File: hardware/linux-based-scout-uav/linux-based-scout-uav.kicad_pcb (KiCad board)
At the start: 2 copper layers, 70 x 100 mm, 40 parts, among them J1 XT60PW-M, J2 Micro_SD_Card_Det2, J3 TC2050-IDC-NL, J4 0786463001, J5 GSB1C41110SSHR, Q1 DMP3013SFV, Q2 DMP3013SFV, U1 OSD32MP157C-512M-IAA, U10 G313-06329-00, U2 RN2903A-I_RM098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

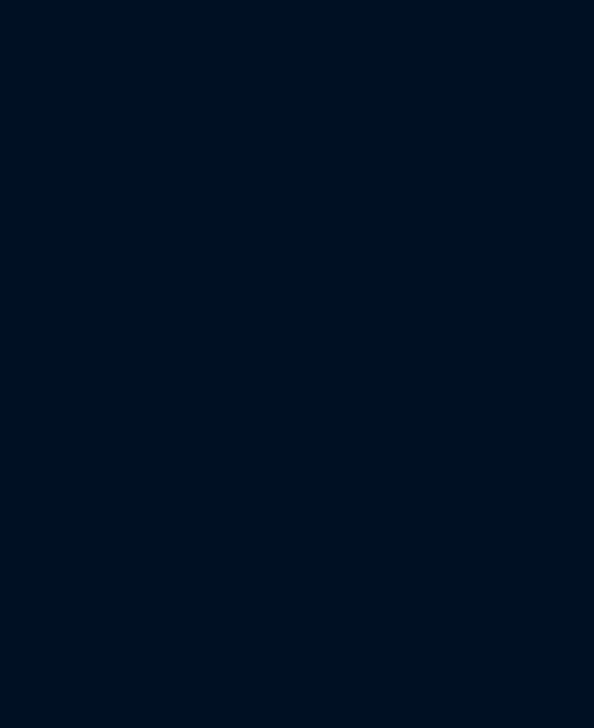
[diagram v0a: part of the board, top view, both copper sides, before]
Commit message: Schematic update - added Google Coral
Google Coral edge TPU added to schematic
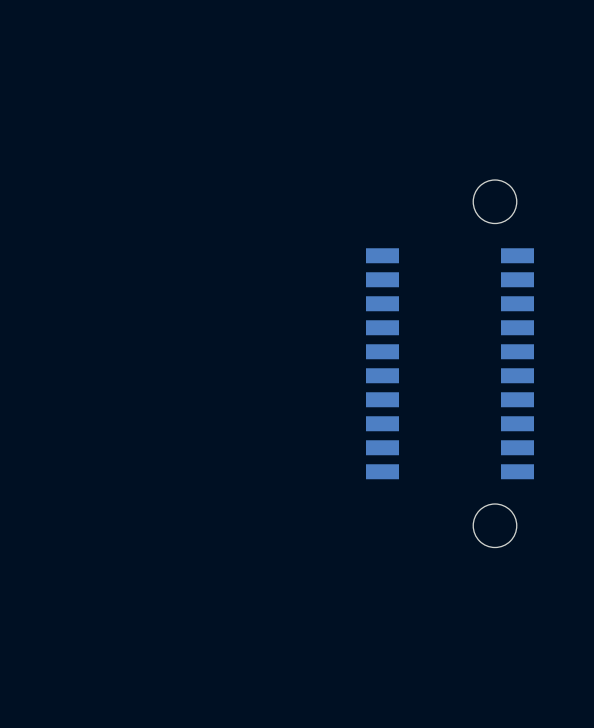
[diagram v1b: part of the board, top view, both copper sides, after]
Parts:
- added J6: ERF8-010-05.0-L-DV-K-TR, ERF8-010-05.0-L-DV-K-TR:SAMTEC_ERF8-010-05.0-L-DV-K-TR, B.Cu at (190.2, 122.2)

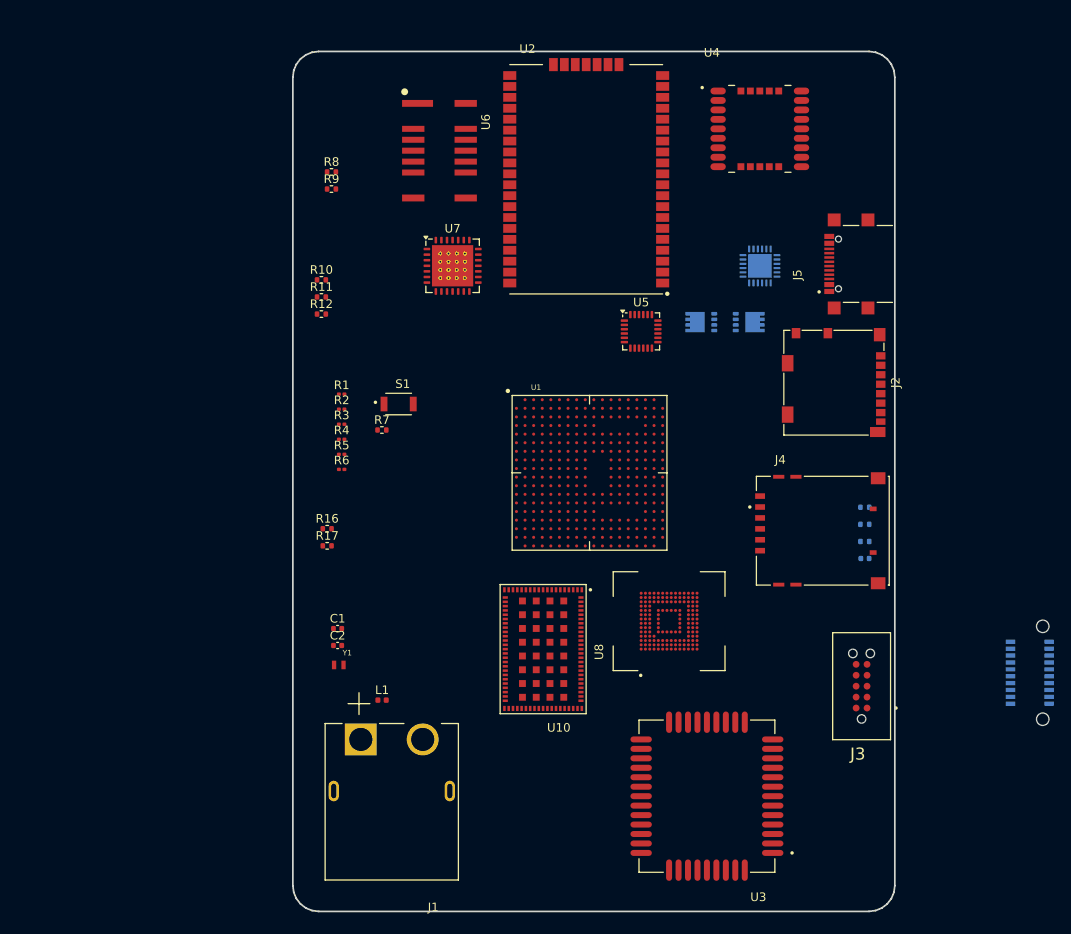
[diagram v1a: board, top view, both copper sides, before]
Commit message: Schematic, board update
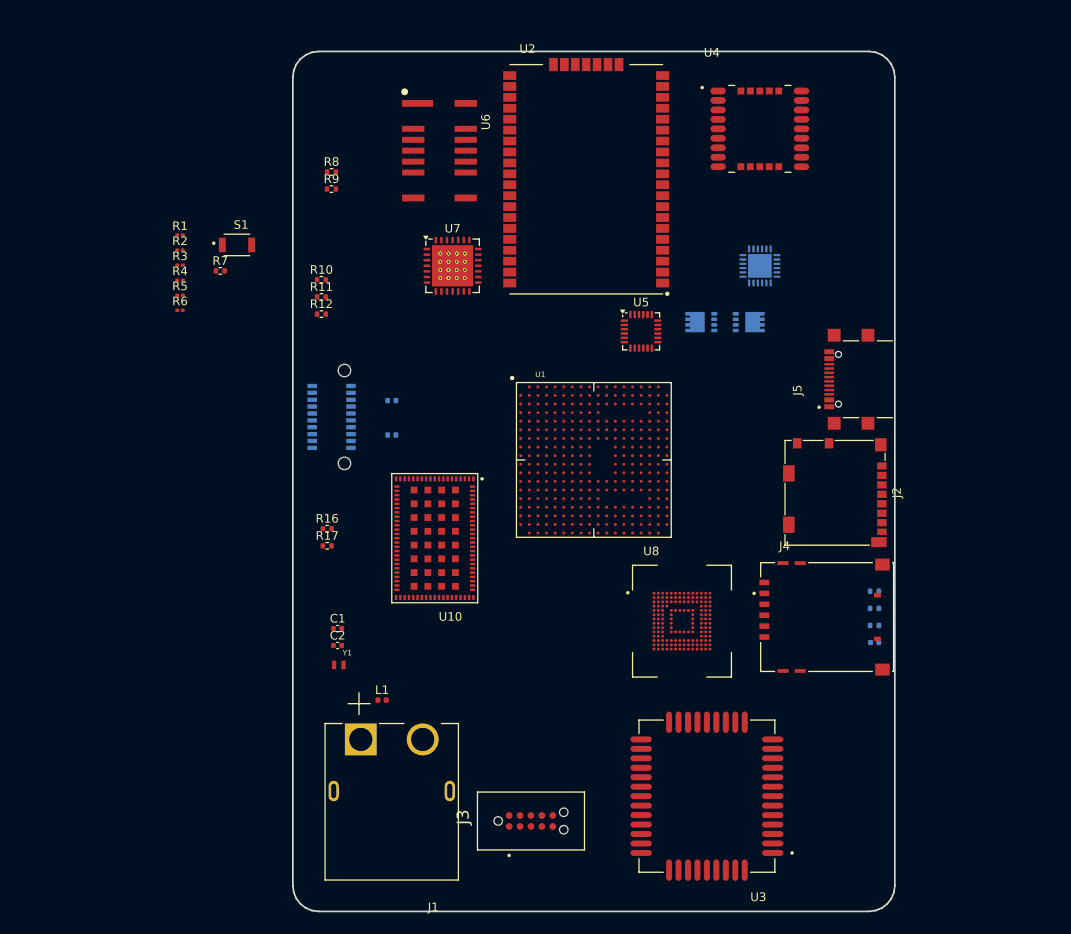
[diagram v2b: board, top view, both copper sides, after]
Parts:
- added C13: 100nF, Capacitor_SMD:C_0402_1005Metric, B.Cu at (116.0, 90.6)
- added C14: 100nF, Capacitor_SMD:C_0402_1005Metric, B.Cu at (116.0, 94.6)
- moved J6 86.5 mm to (109.0, 92.5)
- moved J3 43.8 mm to (129.7, 140.1), turned to 90 degrees
- moved R1 26.4 mm to (91.4, 71.3)
- moved R2 26.4 mm to (91.4, 73.1)
- moved R3 26.4 mm to (91.4, 74.8)
- moved R4 26.4 mm to (91.4, 76.6)
- moved R5 26.4 mm to (91.4, 78.3)
- moved R6 26.4 mm to (91.4, 80.1)
- moved R7 26.4 mm to (96.1, 75.5)
- moved S1 26.4 mm to (98.0, 72.5)
- moved U10 18.0 mm to (121.0, 106.6)
- moved J5 13.4 mm to (170.6, 88.1)
- moved J2 12.8 mm to (167.6, 101.3)
- moved J4 10.1 mm to (166.6, 115.8)
- moved C3 9.83 mm to (172.2, 118.7)
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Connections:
- J6 pad 01: unconnected-(J6-Pad01) -> GND
- J6 pad 02: unconnected-(J6-Pad02) -> GND
- J6 pad 04: unconnected-(J6-Pad04) -> PCIE_RX_N
- J6 pad 06: unconnected-(J6-Pad06) -> PCIE_RX_P
- J6 pad 08: unconnected-(J6-Pad08) -> GND
- J6 pad 10: unconnected-(J6-Pad10) -> PCIE_TX_P
- J6 pad 12: unconnected-(J6-Pad12) -> PCIE_TX_N
- J6 pad 14: unconnected-(J6-Pad14) -> GND
- J6 pad 16: unconnected-(J6-Pad16) -> PCIE_REFCLK_N
- J6 pad 18: unconnected-(J6-Pad18) -> PCIE_REFCLK_P
- J6 pad 19: unconnected-(J6-Pad19) -> GND
- J6 pad 20: unconnected-(J6-Pad20) -> GND
- U10 pad 10: unconnected-(U10-PCIE_REFCLK_N-Pad10) -> PCIE_REFCLK_N
- U10 pad 11: unconnected-(U10-PCIE_REFCLK_P-Pad11) -> PCIE_REFCLK_P
- U10 pad 4: unconnected-(U10-PCIE_TX_N-Pad4) -> /google-tpu-coral-1/H_PCIE_TX_N
- U10 pad 5: unconnected-(U10-PCIE_TX_P-Pad5) -> /google-tpu-coral-1/H_PCIE_TX_P
- U10 pad 7: unconnected-(U10-PCIE_RX_P-Pad7) -> PCIE_RX_P
- U10 pad 8: unconnected-(U10-PCIE_RX_N-Pad8) -> PCIE_RX_N

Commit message: Schematic and Board update
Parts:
- added TP20: TestPoint, TestPoint:TestPoint_Pad_D1.0mm, F.Cu at (97.5, 48.5)
- added TP21: TestPoint, TestPoint:TestPoint_Pad_D1.0mm, F.Cu at (97.5, 53.0)
- added TP22: TestPoint, TestPoint:TestPoint_Pad_D1.0mm, F.Cu at (97.5, 57.6)
- added TP23: TestPoint, TestPoint:TestPoint_Pad_D1.0mm, F.Cu at (97.5, 62.1)
- added TP24: TestPoint, TestPoint:TestPoint_Pad_D1.0mm, F.Cu at (97.5, 66.7)
- moved U6 1.50 mm to (120.0, 61.5)
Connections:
- U2 pad 35: unconnected-(U2-GPIO0-Pad35) -> Net-(U2-GPIO0)
- U2 pad 36: unconnected-(U2-GPIO1-Pad36) -> Net-(U2-GPIO1)
- U2 pad 37: unconnected-(U2-GPIO2-Pad37) -> Net-(U2-GPIO2)
- U2 pad 38: unconnected-(U2-GPIO3-Pad38) -> Net-(U2-GPIO3)
- U2 pad 39: unconnected-(U2-GPIO4-Pad39) -> Net-(U2-GPIO4)
- U2 pad 6: unconnected-(U2-UART_TX-Pad6) -> UART_TX
- U2 pad 7: unconnected-(U2-UART_RX-Pad7) -> UART_RX

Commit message: Added TPS65217C PMIC
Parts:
- added U11: TPS65217CRSLR, TPS65217CRSLR:IC_TPS65217CRSLR, F.Cu at (76.5, 92.3)

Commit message: Update
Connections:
- U11 pad 30: Net-(U11-PGND-Pad30) -> GND
- U11 pad 41: unconnected-(U11-AGND-Pad41) -> GND
- U11 pad 49: Net-(U11-PGND-Pad30) -> GND
- U11 pad 50: Net-(U11-PGND-Pad30) -> GND
- U11 pad 51: Net-(U11-PGND-Pad30) -> GND
- U11 pad 52: Net-(U11-PGND-Pad30) -> GND
- U11 pad 53: Net-(U11-PGND-Pad30) -> GND
- U11 pad 54: Net-(U11-PGND-Pad30) -> GND
- U11 pad 55: Net-(U11-PGND-Pad30) -> GND
- U11 pad 56: Net-(U11-PGND-Pad30) -> GND
- U11 pad 57: Net-(U11-PGND-Pad30) -> GND
- U11 pad 58: Net-(U11-PGND-Pad30) -> GND
- U11 pad 59: Net-(U11-PGND-Pad30) -> GND
- U11 pad 60: Net-(U11-PGND-Pad30) -> GND
- U11 pad 61: Net-(U11-PGND-Pad30) -> GND
- U11 pad 62: Net-(U11-PGND-Pad30) -> GND
- U11 pad 63: Net-(U11-PGND-Pad30) -> GND
- U11 pad 64: Net-(U11-PGND-Pad30) -> GND
- U11 pad 65: Net-(U11-PGND-Pad30) -> GND

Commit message: Updated project to KiCad 9.0
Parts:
- added R36: 49.9K, Resistor_SMD:R_0402_1005Metric, F.Cu at (181.0, 77.0)
- added R37: 10K, Resistor_SMD:R_0402_1005Metric, F.Cu at (181.0, 79.0)
- moved U11 5.32 mm to (81.7, 93.5)
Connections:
- Q1 pad 4: unconnected-(Q1-G-Pad4) -> Net-(Q1-G)
- Q1 pad 5: unconnected-(Q1-D-Pad5) -> +VBUS
- Q2 pad 1: Net-(Q2-S-Pad1) -> Net-(Q1-S-Pad1)
- Q2 pad 2: Net-(Q2-S-Pad1) -> Net-(Q1-S-Pad1)
- Q2 pad 3: Net-(Q2-S-Pad1) -> Net-(Q1-S-Pad1)
- Q2 pad 4: unconnected-(Q2-G-Pad4) -> Net-(Q1-G)
- Q2 pad 5: unconnected-(Q2-D-Pad5) -> PD_VBUS
